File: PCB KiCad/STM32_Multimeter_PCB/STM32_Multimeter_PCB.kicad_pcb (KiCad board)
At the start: 4 copper layers, 55.2 x 76.5 mm, 129 parts, among them J1 Conn_01x02_Pin, J10 Conn_01x01_Pin, J11 Conn_01x01_Pin, J2 USB_B_Micro, J3 Conn_01x04_Pin, J4 Conn_Coaxial, J5 Conn_01x03_Pin, J7 Conn_01x02_Pin, J8 Conn_01x01_Pin, K1 G6K-2, Q1 AOD2810, Q10 BC327, Q11 BC327, Q12 BC327, Q13 BC327, Q14 BC327, Q15 BC327, Q2 AOD2810, Q3 AOD2810, Q4 AOD2810, Q5 AOD2810, Q6 BC327, Q7 BC327, Q8 BC327, Q9 BC327, SW4 SW_DPDT_x2, U1 STM32WB55CGUx, U10 AMS1117-3.3, U11 4051, U3 LTC4054XES5-4.2, U4 DW01A, U5 FS8205A, U9 TPS61040DBV, Y1 Crystal 32 MHz

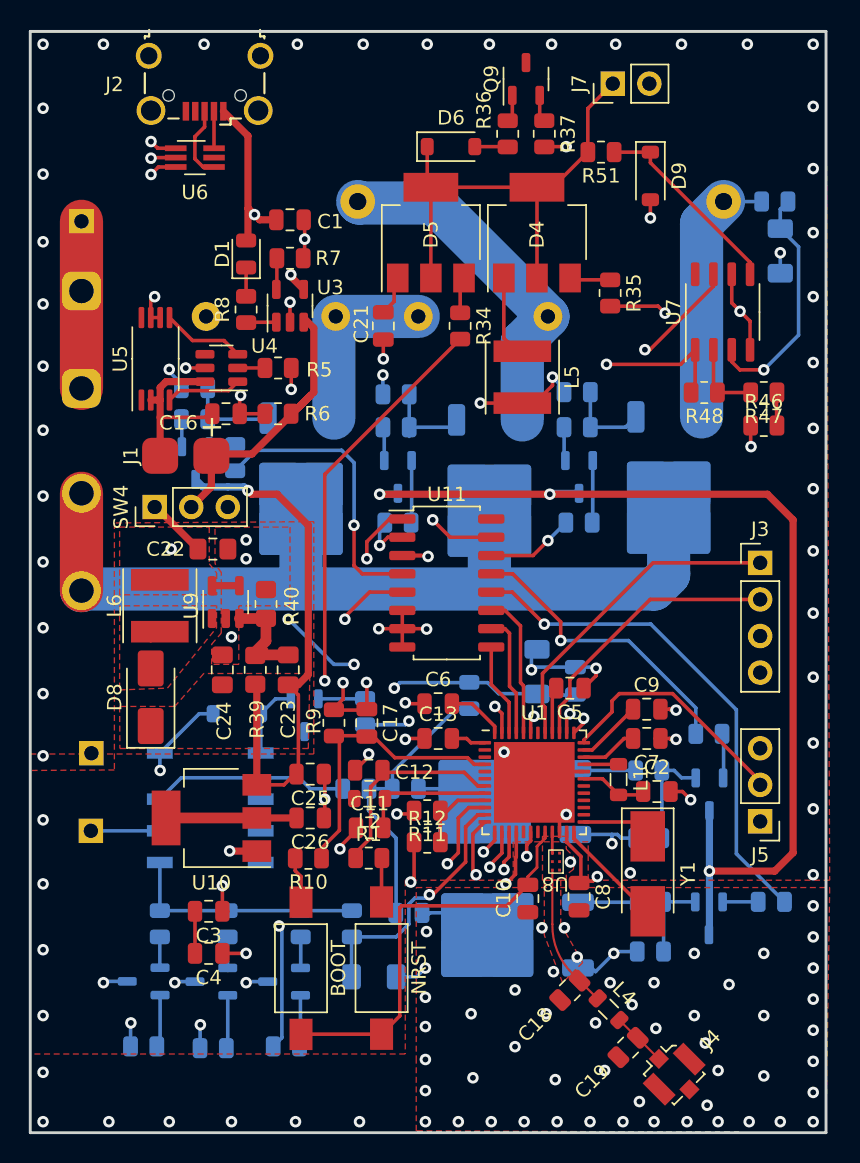
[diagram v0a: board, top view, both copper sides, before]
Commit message: added i2c for oled and 2 buttons to pcb
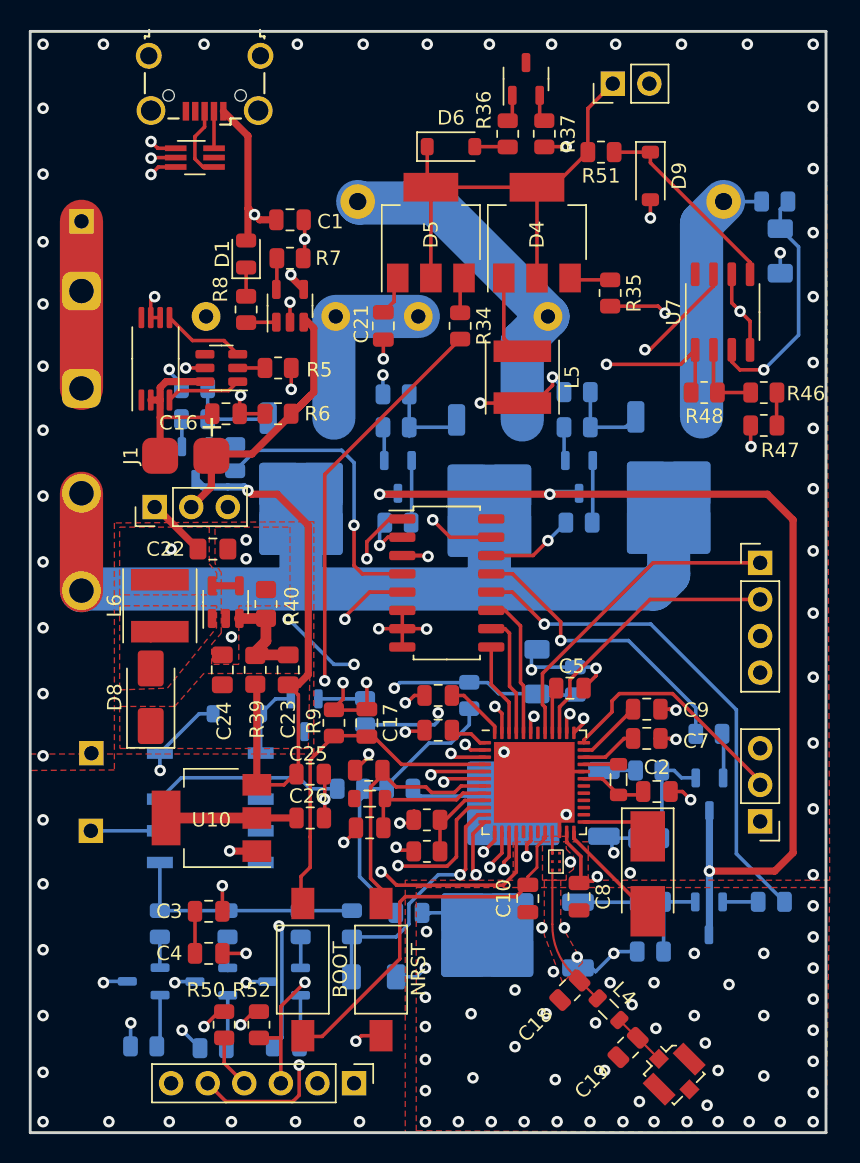
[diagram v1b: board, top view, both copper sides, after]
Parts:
- removed R1, R10: 100R, Resistor_SMD:R_0805_2012Metric
- added J9: Conn_01x06_Pin, Connector_PinHeader_2.54mm:PinHeader_1x06_P2.54mm_Vertical, F.Cu at (53.5, 93.3)
- added R50: 2k R, Resistor_SMD:R_0805_2012Metric, F.Cu at (44.5, 89.3)
- added R52: 2k R, Resistor_SMD:R_0805_2012Metric, F.Cu at (46.9, 89.3)
- BOOT: value SW_Push -> BOOT
- NRST: value SW_Push -> NRST
- moved Q1 1.99 mm to (65.8, 73.9)
- moved R11 0.64 mm to (58.5, 75.1)
- moved R12 0.64 mm to (58.5, 77.2)
- moved C13 0.57 mm to (59.3, 68.8)
- moved C6 0.57 mm to (59.3, 66.4)
- moved R14 0.38 mm to (53.2, 72.9)
- moved R20 0.38 mm to (56.6, 72.9)
- moved BOOT 0.16 mm to (49.9, 85.5)
- moved NRST 0.11 mm to (55.3, 85.5)
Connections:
- BOOT pad 1: Net-(R10-Pad2) -> Net-(U1-PH3)
- NRST pad 1: Net-(R1-Pad2) -> Net-(U1-NRST)
- NRST pad 2: VDD -> GND
- U1 pad 2: unconnected-(U1-PC14-Pad2) -> BU1
- U1 pad 3: unconnected-(U1-PC15-Pad3) -> BU2
- U1 pad 5: unconnected-(U1-PB8-Pad5) -> Net-(J9-Pin_3)
- U1 pad 6: unconnected-(U1-PB9-Pad6) -> Net-(J9-Pin_4)
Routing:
- net BU2: track 0.00 -> 38.2 mm, vias 0 -> 2
- net BU1: track 0.00 -> 36.0 mm, vias 0 -> 1
- net Net-(J9-Pin_4): track 0.00 -> 33.5 mm, vias 0 -> 1
- net Net-(J9-Pin_3): track 0.00 -> 31.8 mm, vias 0 -> 2
- net Net-(U1-NRST): track 13.7 -> 17.4 mm
- net Net-(U1-PH3): track 20.3 -> 23.6 mm
- net Net-(R10-Pad2): track 3.21 -> 0.00 mm
- net Net-(R1-Pad2): track 3.06 -> 0.00 mm
- net voltage input: track 32.9 -> 35.6 mm
- net VDD: track 70.9 -> 68.7 mm
- net GND: track 100.3 -> 102.4 mm, vias 140 -> 143
- net Net-(Q1-G): track 4.23 -> 2.21 mm
- net C on: track 53.8 -> 55.4 mm
- net BATT sens: track 5.12 -> 6.36 mm
- net Range 100 to 10k ohm: track 39.5 -> 40.5 mm
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
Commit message: added pin names to silkscreen
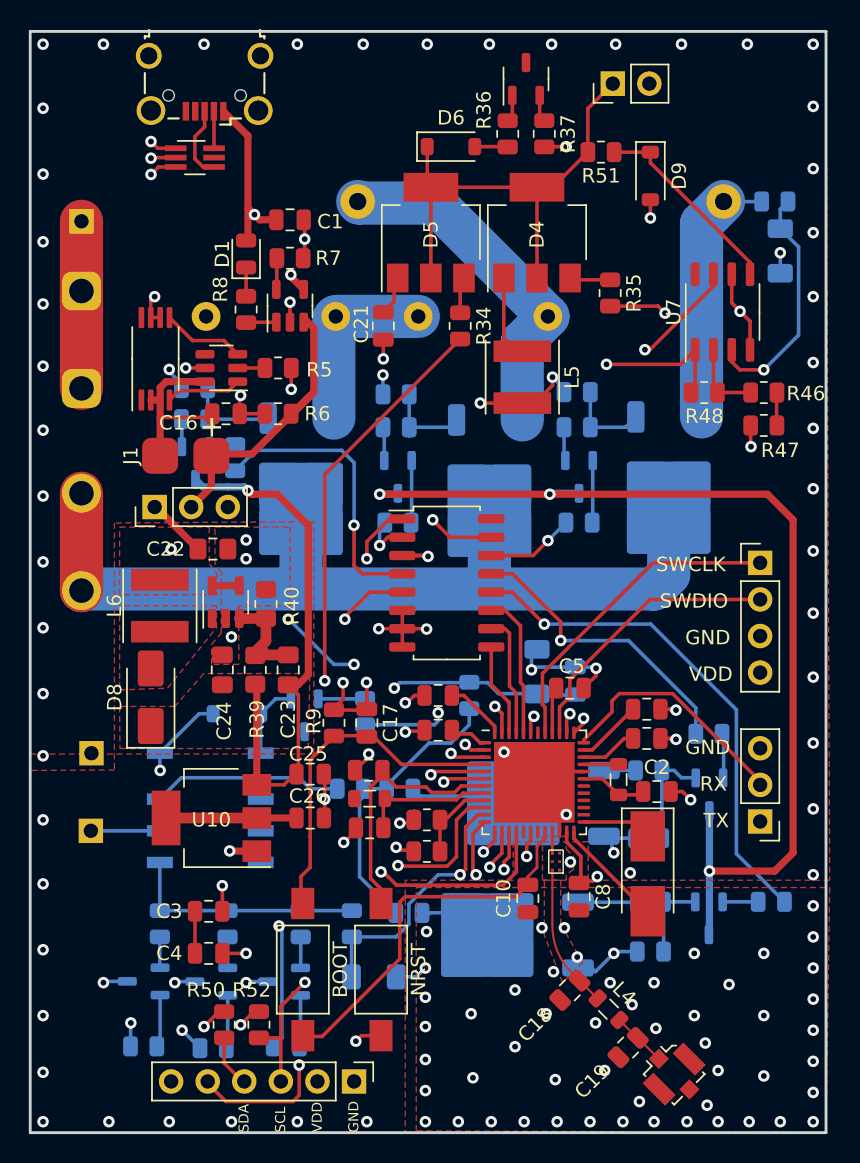
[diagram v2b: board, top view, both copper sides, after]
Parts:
- moved J9 0.13 mm to (53.5, 93.2)
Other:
- board text added: "GND"
- board text added: "RX"
- board text added: "SCL"
- board text added: "SDA"
- board text added: "SWCLK"
- board text added: "SWDIO"
- board text added: "TX"
- board text added: "VDD"
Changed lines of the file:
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@@
     (property "ki_keywords" "cap capacitor")
     (attr smd)
-    (fp_text reference "C9" (at 3.429 0.062) (layer "F.SilkS")
+    (fp_text reference "C9" (at 3.429 0.062) (layer "F.SilkS") hide
         (effects (font (size 1 1) (thickness 0.15)))
     )
@@
     (property "ki_keywords" "cap capacitor")
     (attr smd)
-    (fp_text reference "C7" (at -3.429 -0.189) (layer "F.SilkS")
+    (fp_text reference "C7" (at -3.429 -0.189) (layer "F.SilkS") hide
         (effects (font (size 1 1) (thickness 0.15)))
     )
@@
   )
   (footprint "Connector_PinHeader_2.54mm:PinHeader_1x06_P2.54mm_Vertical" (layer "F.Cu")
-    (at 53.467 93.345 -90)
+    (at 53.467 93.218 -90)
     (descr "Through hole straight pin header, 1x06, 2.54mm pitch, single row")
     (tags "Through hole pin header THT 1x06 2.54mm single row")
@@
   (gr_rect (start 30.988 20.32) (end 86.233 96.774)
     (stroke (width 0.2) (type default)) (fill none) (layer "Edge.Cuts"))
+  (gr_text "VDD" (at 76.708 65.532) (layer "F.SilkS")
+    (effects (font (size 1 1) (thickness 0.15)) (justify left bottom))
+  )
+  (gr_text "GND" (at 53.848 96.774 90) (layer "F.SilkS")
+    (effects (font (size 0.7 0.7) (thickness 0.15)) (justify left bottom))
+  )
+  (gr_text "GND" (at 76.454 62.992) (layer "F.SilkS")
+    (effects (font (size 1 1) (thickness 0.15)) (justify left bottom))
+  )
+  (gr_text "GND" (at 76.454 70.612) (layer "F.SilkS")
+    (effects (font (size 1 1) (thickness 0.15)) (justify left bottom))
+  )
+  (gr_text "VDD\n" (at 51.308 96.774 90) (layer "F.SilkS")
+    (effects (font (size 0.7 0.7) (thickness 0.15)) (justify left bottom))
+  )
+  (gr_text "TX" (at 77.724 75.692) (layer "F.SilkS")
+    (effects (font (size 1 1) (thickness 0.15)) (justify left bottom))
+  )
+  (gr_text "SWDIO" (at 74.676 60.452) (layer "F.SilkS")
+    (effects (font (size 1 1) (thickness 0.15)) (justify left bottom))
+  )
+  (gr_text "SCL" (at 48.768 96.774 90) (layer "F.SilkS")
+    (effects (font (size 0.7 0.7) (thickness 0.15)) (justify left bottom))
+  )
+  (gr_text "RX" (at 77.47 73.152) (layer "F.SilkS")
+    (effects (font (size 1 1) (thickness 0.15)) (justify left bottom))
+  )
+  (gr_text "SDA" (at 46.228 96.774 90) (layer "F.SilkS")
+    (effects (font (size 0.7 0.7) (thickness 0.15)) (justify left bottom))
+  )
+  (gr_text "SWCLK" (at 74.422 57.912) (layer "F.SilkS")
+    (effects (font (size 1 1) (thickness 0.15)) (justify left bottom))
+  )
   (segment (start 79.6885 39.169) (end 79.8155 39.296) (width 0.25) (layer "F.Cu") (net 1))
   (segment (start 50.038 34.743751) (end 50.038 35.6705) (width 0.25) (layer "F.Cu") (net 1))
@@
   (via (at 31.877 70.612) (size 0.8) (drill 0.4) (layers "F.Cu" "B.Cu") (free) (net 1))
   (via (at 83.058 35.687) (size 0.8) (drill 0.4) (layers "F.Cu" "B.Cu") (free) (net 1))
-  (via (at 49.403 96.012) (size 0.8) (drill 0.4) (layers "F.Cu" "B.Cu") (free) (net 1))
+  (via (at 49.53 96.012) (size 0.8) (drill 0.4) (layers "F.Cu" "B.Cu") (free) (net 1))
   (via (at 31.877 34.925) (size 0.8) (drill 0.4) (layers "F.Cu" "B.Cu") (free) (net 1))
   (via (at 85.344 21.209) (size 0.8) (drill 0.4) (layers "F.Cu" "B.Cu") (free) (net 1))
@@
   (via (at 31.877 75.057) (size 0.8) (drill 0.4) (layers "F.Cu" "B.Cu") (free) (net 1))
   (via (at 64.643 86.868) (size 0.8) (drill 0.4) (layers "F.Cu" "B.Cu") (free) (net 1))
-  (via (at 53.848 96.012) (size 0.8) (drill 0.4) (layers "F.Cu" "B.Cu") (free) (net 1))
+  (via (at 54.356 96.012) (size 0.8) (drill 0.4) (layers "F.Cu" "B.Cu") (free) (net 1))
   (via (at 77.089 88.646) (size 0.8) (drill 0.4) (layers "F.Cu" "B.Cu") (free) (net 1))
   (via (at 85.344 91.821) (size 0.8) (drill 0.4) (layers "F.Cu" "B.Cu") (free) (net 1))

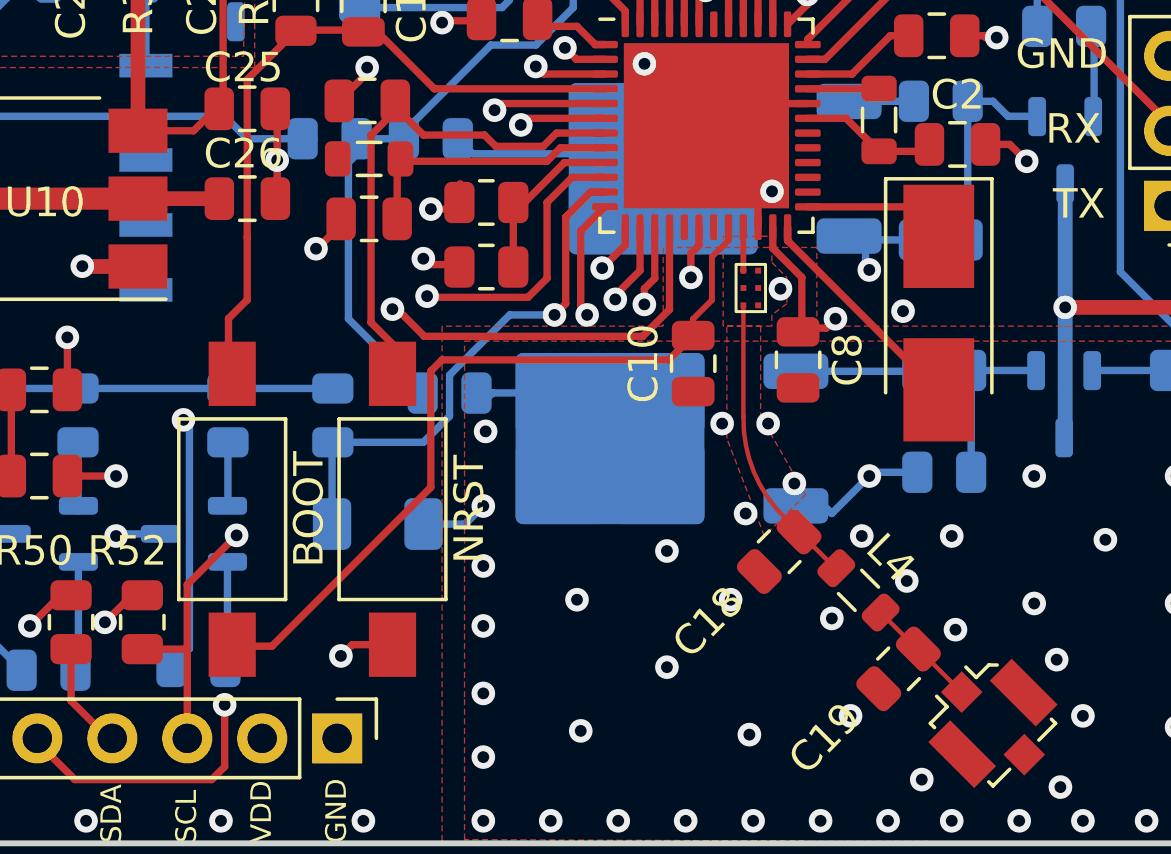
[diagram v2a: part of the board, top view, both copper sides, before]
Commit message: added missing shop links to the part list
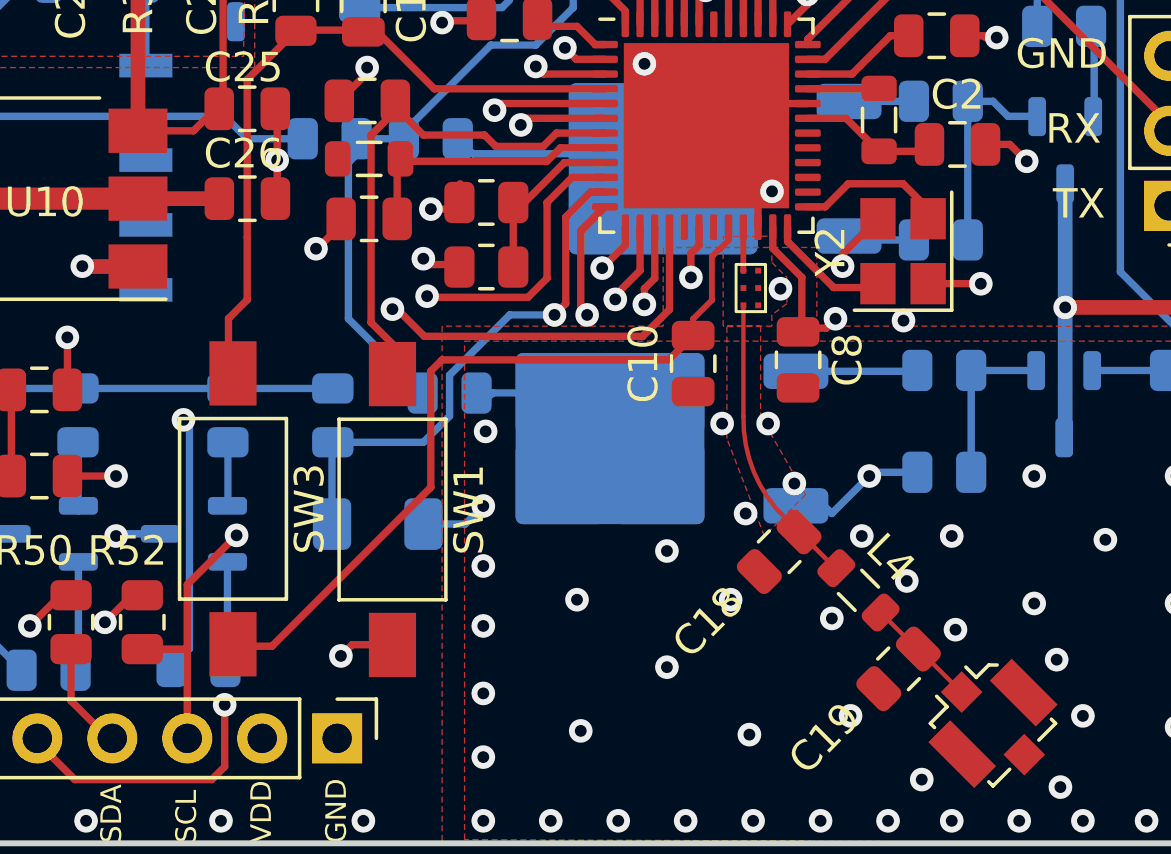
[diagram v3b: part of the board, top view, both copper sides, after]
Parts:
- removed BOOT: BOOT, Button_Switch_SMD:SW_SPST_FSMSM
- removed NRST: NRST, Button_Switch_SMD:SW_SPST_FSMSM
- removed Y1: Crystal 32 MHz, Crystal:Crystal_SMD_5032-2Pin_5.0x3.2mm_HandSoldering
- added SW1: NRST, Button_Switch_SMD:SW_SPST_FSMSM, F.Cu at (55.3, 85.5)
- added SW3: BOOT, Button_Switch_SMD:SW_SPST_FSMSM, F.Cu at (49.9, 85.4)
- added Y2: Crystal_GND24, Crystal:Crystal_SMD_3225-4Pin_3.2x2.5mm, F.Cu at (72.6, 76.7)
- R14: value 900k R -> 910k R
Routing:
- net GND: track 102.4 -> 106.7 mm, vias 143 -> 144
- net Net-(U1-OSC_OUT): track 8.11 -> 4.25 mm
